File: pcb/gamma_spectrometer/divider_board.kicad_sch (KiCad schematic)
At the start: 37 parts, among them Q401 MMBTA42, Q402 MMBTA42, Q403 MMBTA42, U401 AD8000YRDZ-REEL

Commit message: Complete BOM: MPN and footprints for all components
Session 5 (2026-05-23) - full BOM assignment finished.

Components assigned (KiCad Symbol Fields + Footprints):
- 81 capacitors / 17 unique MPN (Yageo, Murata, Vishay, Holy Stone)
- 79 resistors / 28 unique MPN (Yageo RC/RT/RL/AC series)
- 3 inductors (Bourns SRN3015 + SRU5028)
- 2 LEDs (Foryard + Wurth 0805)
- 1 PTC fuse (MF-MSMF050-2)
- 1 ferrite bead (Murata BLM18EG121SN1D, 0603 - fixed from docs 0402)
- All active ICs (STM32G474, MAX1847, AD8000, FT231XQ, etc.)

Key design decisions:
- Standard bypass: 100nF X7R 0603 (easier hand soldering vs 0402)
- LED package 0805 (instead of 0402)
- C115 consolidated with C206 on single MPN (GRM32ER71A476KE15L)
- HV chain (1812 1kV X7R, 18x): Holy Stone C1812X104K102T
- AD8000 Cfb: GRM1555C1H1R0WA01D 1pF +/-0.05pF NP0
- R415: 50R -> 49.9R E96 (50R unavailable in catalog)
- L101/L102: SRN3015 (footprint Neosid SMS-ME3015, geometry verified)
- L103: SRU5028 (footprint L_Bourns_SRU5016, XY identical)

Documentation contradictions fixed:
- C115 MPN: GRM32ER61A476KE20L -> GRM32ER71A476KE15L
- FT231XS (SSOP-16) -> FT231XQ (QFN-20) - actual chip choice
- Tantalum MPN: TAJA106K016RNJ -> TR3B106K010C0750 (Vishay Low ESR)
- Inductor refs in usb_power_board_schematic.md updated

Remaining for PCB order:
- D202/D203 footprint: change SOD-123W -> SOD-123 (Diotec standard)
- J_PMT401: custom B14-38 footprint (during PCB layout)

Files:
- bom_fp_work.md - authoritative BOM with status, MPN, footprints, URLs
- pcb/gamma_spectrometer.net - fresh netlist with all MPN fields
- docs/session_context.md - session 5 final state

Co-Authored-By: Claude Sonnet 4.6 <noreply@anthropic.com>
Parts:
- C401, C402, C403, C404, C405, C406, C407, C410: value 100nF -> 0.1uF; footprint (none) -> Capacitor_SMD:C_1812_4532Metric_Pad1.57x3.40mm_HandSolder; PN (none) -> C1812X104K102T; Ссылка на покупку  (none) -> https://www.electronshik.ru/item/HOLY/C1812X104K102T
- C408: footprint (none) -> Capacitor_SMD:C_1210_3225Metric_Pad1.33x2.70mm_HandSolder; PN (none) -> CC1210KKX7RCBB223; Ссылка на покупку  (none) -> https://www.electronshik.ru/item/YAG/CC1210KKX7RCBB223
- C409: footprint (none) -> Capacitor_SMD:C_1812_4532Metric_Pad1.57x3.40mm_HandSolder; PN (none) -> GRM43DR73A473KW01L; Ссылка на покупку  (none) -> https://www.electronshik.ru/item/MUR/GRM43DR73A473KW01L
- C411, C413: footprint (none) -> Capacitor_SMD:C_0805_2012Metric_Pad1.18x1.45mm_HandSolder; PN (none) -> GRM21BR61C475KA88L; Ссылка на покупку  (none) -> https://www.electronshik.ru/item/MUR/GRM21BR61C475KA88L
- C412, C414: value 100nF -> 0.1uF; footprint (none) -> Capacitor_SMD:C_0603_1608Metric_Pad1.08x0.95mm_HandSolder; PN (none) -> CC0603JRX7R9BB104; Ссылка на покупку  (none) -> https://www.electronshik.ru/item/YAG/CC0603JRX7R9BB104
- C415: footprint (none) -> Capacitor_SMD:C_0402_1005Metric_Pad0.74x0.62mm_HandSolder; PN (none) -> GRM1555C1H1R0WA01D; Ссылка на покупку  (none) -> https://www.electronshik.ru/item/MUR/GRM1555C1H1R0WA01D
- Q401, Q402, Q403: PN (none) -> MMBTA42; Ссылка на покупку  (none) -> https://www.electronshik.ru/item/DIOTEC/MMBTA42
- R401, R402: footprint (none) -> Resistor_SMD:R_1206_3216Metric_Pad1.30x1.75mm_HandSolder; PN (none) -> RC1206FR-07750KL; Ссылка на покупку  (none) -> https://www.electronshik.ru/item/YAG/RC1206FR-07750KL
- R403, R404, R405, R406, R407: footprint (none) -> Resistor_SMD:R_1206_3216Metric_Pad1.30x1.75mm_HandSolder; PN (none) -> RC1206FR-07680KL; Ссылка на покупку  (none) -> https://www.electronshik.ru/item/YAG/RC1206FR-07680KL
- R408, R411, R413: footprint (none) -> Resistor_SMD:R_0603_1608Metric_Pad0.98x0.95mm_HandSolder; PN (none) -> RC0603FR-0710KL; Ссылка на покупку  (none) -> https://www.electronshik.ru/item/YAG/RC0603FR-0710KL
- R409: footprint (none) -> Resistor_SMD:R_1206_3216Metric_Pad1.30x1.75mm_HandSolder; PN (none) -> RC1206FR-07820KL; Ссылка на покупку  (none) -> https://www.electronshik.ru/item/YAG/RC1206FR-07820KL
- R410: footprint (none) -> Resistor_SMD:R_1206_3216Metric_Pad1.30x1.75mm_HandSolder; PN (none) -> RC1206FR-071ML; Ссылка на покупку  (none) -> https://www.electronshik.ru/item/YAG/RC1206FR-071ML
- R412, R414: footprint (none) -> Resistor_SMD:R_1206_3216Metric_Pad1.30x1.75mm_HandSolder; PN (none) -> RC1206FR-07499KL; Ссылка на покупку  (none) -> https://www.electronshik.ru/item/YAG/RC1206FR-07499KL
- R415: value 50 -> 49.9; footprint (none) -> Resistor_SMD:R_0603_1608Metric_Pad0.98x0.95mm_HandSolder; PN (none) -> RC0603FR-0749R9L; Ссылка на покупку  (none) -> https://www.electronshik.ru/item/YAG/RC0603FR-0749R9L
- R416: footprint (none) -> Resistor_SMD:R_0603_1608Metric_Pad0.98x0.95mm_HandSolder; PN (none) -> RC0603FR-07100RL; Ссылка на покупку  (none) -> https://www.electronshik.ru/item/YAG/RC0603FR-07100RL
- R417: footprint (none) -> Resistor_SMD:R_0603_1608Metric_Pad0.98x0.95mm_HandSolder; PN (none) -> RC0603FR-071K5L; Ссылка на покупку  (none) -> https://www.electronshik.ru/item/YAG/RC0603FR-071K5L
- U401: PN (none) -> AD8000YRDZ-REEL

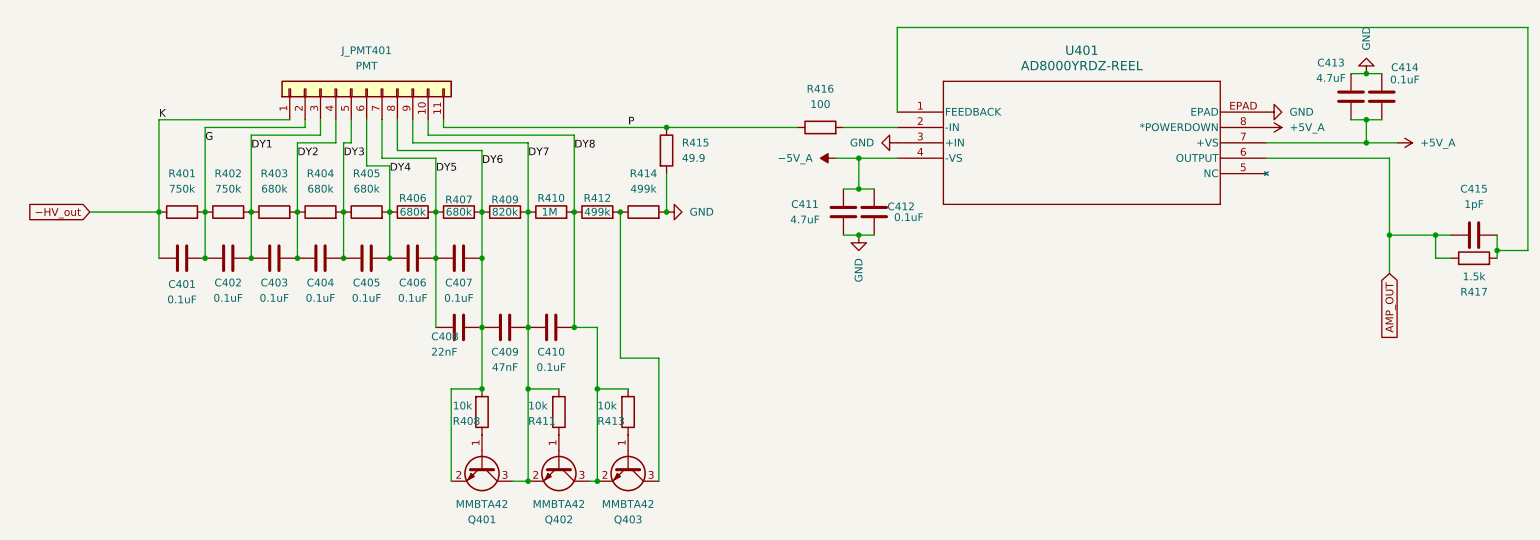
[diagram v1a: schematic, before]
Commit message: Fix 2 critical schematic bugs found by full netlist audit
Full audit of all 191 nets (sessions 7-8, 2026-06-10/11) against design docs.

CRITICAL FIXES (schematic + netlist):
1. UART was straight-through, not crossed: FTDI TXD tied to PA9 (both
   outputs), RXD to PA10 (both inputs) - no communication possible.
   ERC missed it (MCU pins are bidirectional). Now: PA9(TX)->UART_RX
   ->FTDI RXD, FTDI TXD->UART_TX->PA10(RX).
2. PMT divider active buffers were dead: chain junctions were merged
   with dynodes DY6/7/8, so base resistors bridged base to own emitter
   (Vbe=0 forever, MMBTA42 never conducts). Now: dynode = emitter only;
   chain junction -> base resistor -> base; storage caps between dynode
   lines; collectors one stage up. Control nets listed in divider_board.md.
3. R301: 470 -> 330 ohm (ratiometric Pt1000 added 0.225mA load on TL431
   cathode; remaining current was at the 1mA minimum).

Also:
- Pt1000 connected ratiometrically (R303 pullup from TL431 cathode) -
  reference drift cancels out of temperature measurement
- R414 chain bottom goes to GND directly (not via anode/Rin) - docs
  updated to match schematic (cleaner: divider current bypasses signal node)
- cheatsheet_mistakes.md: new rules #7 (UART cross), #8 (dynode=emitter
  only), #9 (recalculate TL431 cathode current when loading VREF node)
- New docs: ad4084_dpp_design.md (v2 DPP upgrade spec, deferred),
  reference_spectra.md (baseline spectra analysis from user's current
  Sypher spectrometer: Cs-137, Lu-176, Am-241, Ra-226, Th-232)
- Datasheets added: AD4084, LTC2387-16/18
- Session context updated (sessions 7-8)

Known leftover: R301 purchase URL in KiCad still points to 470RL part.

Co-Authored-By: Claude Fable 5 <noreply@anthropic.com>
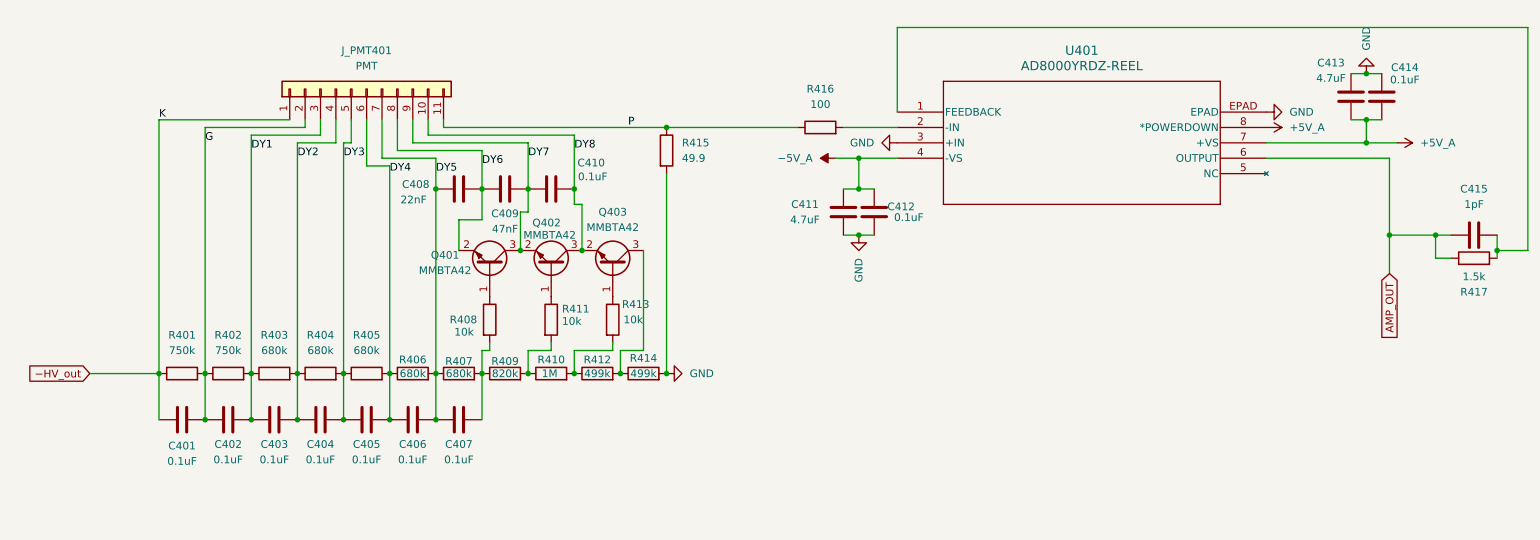
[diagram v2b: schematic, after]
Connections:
- net DY6: no longer C407.2, R407.2, R408.2, R409.1
- net DY7: no longer R409.2, R410.1, R411.2
- net DY8: no longer R410.2, R412.1, R413.2
- new net: C407.2, R407.2, R408.2, R409.1
- new net: R410.2, R412.1, R413.2
- new net: R409.2, R410.1, R411.2
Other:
- moved on the sheet: C401, C402, C403, C404, C405, C406, C407, C408, C409, C410, Q401, Q402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

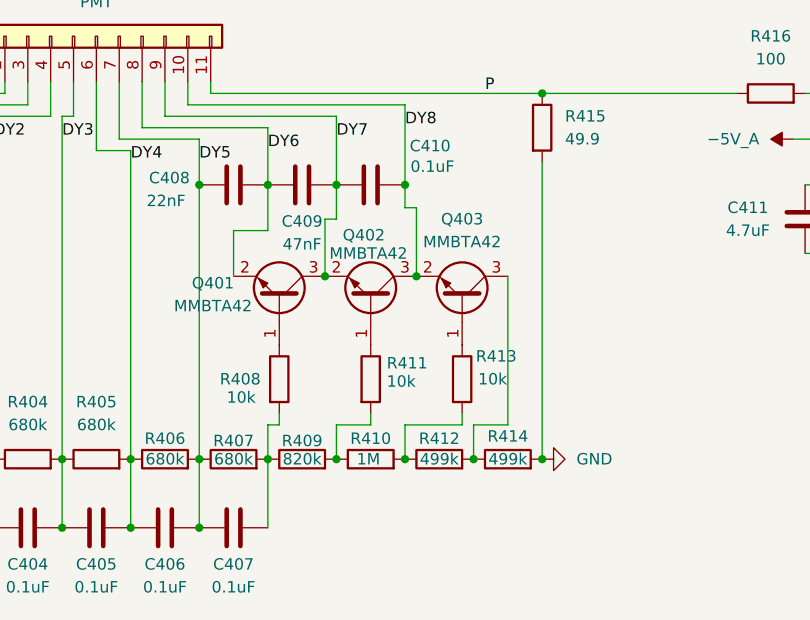
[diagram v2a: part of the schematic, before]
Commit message: pcb: интеграция фикса C1 — Q403→GND, R414 убран, R412→1M + проверка
Пользователь интегрировал C1 в divider_board: коллектор Q403 на GND, R414 удалён,
R412 499k→1M (слияние R412+R414, узел midP исключён). Проверено по нетлисту:
R412=1M cd8↔GND, R414 отсутствует, Q403.C→GND — верно.

DUT (dut_divider.cir) обновлён под as-built топологию; перемерено на замороженном
стенде: сдвиг усиления -0.144%, T_C1 PASS (как и предложенный фикс — слияние эквивалентно).

⚠ BOM ещё НЕ перегенерён (строка R412,R414@499k устарела) — нужен повтор экспорта
(R414 убрать, R412→1M). До этого C1 в железе не полностью закрыт (как было с R314/C2).

Co-Authored-By: Claude Opus 4.8 <noreply@anthropic.com>
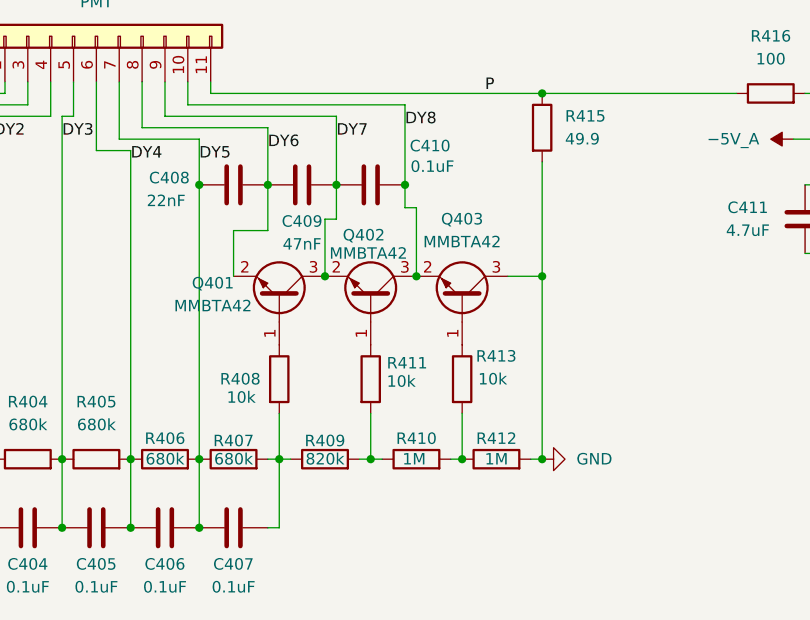
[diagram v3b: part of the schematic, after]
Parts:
- removed R414: 499k, Resistor_SMD:R_1206_3216Metric_Pad1.30x1.75mm_HandSolder, symbol Device:R
- R412: value 499k -> 1M; PN RC1206FR-07499KL -> RC1206FR-071ML; Ссылка на покупку  https://www.electronshik.ru/item/YAG/RC1206FR-07499KL -> https://www.electronshik.ru/item/YAG/RC1206FR-071ML
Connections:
- net GND: now also Q403.3 (C), R412.2
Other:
- moved on the sheet: R409, R410, R412
